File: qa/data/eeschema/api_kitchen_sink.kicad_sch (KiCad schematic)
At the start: 1 part

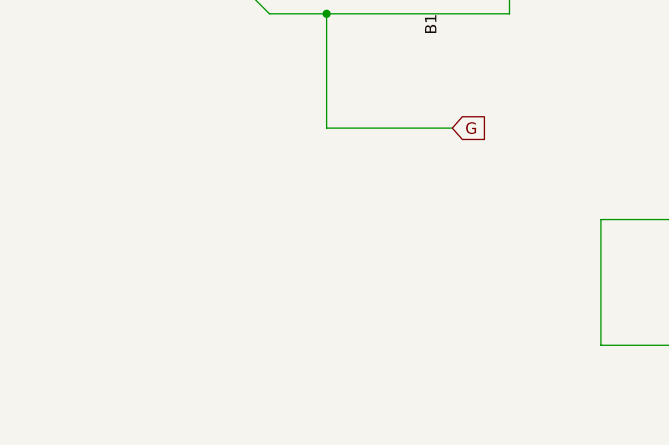
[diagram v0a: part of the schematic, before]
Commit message: API: support symbols and pins
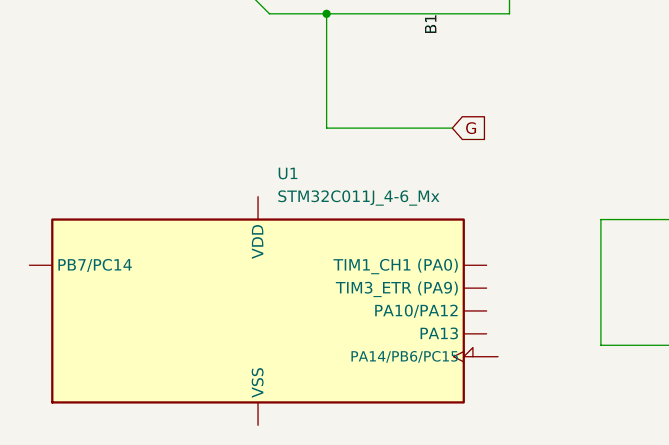
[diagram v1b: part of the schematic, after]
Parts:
- added U1: STM32C011J_4-6_Mx, Package_SO:SOIC-8_3.9x4.9mm_P1.27mm, symbol MCU_ST_STM32C0:STM32C011J_4-6_Mx
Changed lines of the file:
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@@
+	)
+	(symbol
+		(lib_id "MCU_ST_STM32C0:STM32C011J_4-6_Mx")
+		(at 52.07 73.66 0)
+		(unit 1)
+		(body_style 1)
+		(exclude_from_sim no)
+		(in_bom yes)
+		(on_board yes)
+		(in_pos_files no)
+		(dnp no)
+		(fields_autoplaced yes)
+		(property "Reference" "U1"
+			(at 54.2133 58.42 0)
+			(show_name no)
+			(do_not_autoplace no)
+			(effects
+				(font
+					(size 1.27 1.27)
+				)
+				(justify left)
+			)
+		)
+		(property "Value" "STM32C011J_4-6_Mx"
+			(at 54.2133 60.96 0)
+			(show_name no)
+			(do_not_autoplace no)
+			(effects
+				(font
+					(size 1.27 1.27)
+				)
+				(justify left)
+			)
+		)
+		(property "Footprint" "Package_SO:SOIC-8_3.9x4.9mm_P1.27mm"
+			(at 29.21 83.82 0)
+			(hide yes)
+			(show_name no)
+			(do_not_autoplace no)
+			(effects
+				(font
+					(size 1.27 1.27)
+				)
+				(justify right)
+			)
+		)
+		(property "Datasheet" "https://www.st.com/resource/en/datasheet/stm32c011j4.pdf"
+			(at 52.07 73.66 0)
+			(hide yes)
+			(show_name no)
+			(do_not_autoplace no)
+			(effects
+				(font
+					(size 1.27 1.27)
+				)
+			)
+		)
+		(property "Description" "STMicroelectronics Arm Cortex-M0+ MCU, 16-32KB flash, 6KB RAM, 48 MHz, 2.0-3.6V, 6 GPIO, SO8N"
+			(at 52.07 73.66 0)
+			(hide yes)
+			(show_name no)
+			(do_not_autoplace no)
+			(effects
+				(font
+					(size 1.27 1.27)
+				)
+			)
+		)
+		(pin "6"
+		)
+		(pin "7"
+		)
+		(pin "8"
+		)
+		(pin "1"
+		)
+		(pin "2"
+		)
+		(pin "3"
+		)
+		(pin "4"
+			(alternate "TIM1_CH1 (PA0)")
+		)
+		(pin "5"
+			(alternate "TIM3_ETR (PA9)")
+		)
+		(instances
+			(project "api_kitchen_sink"
+				(path "/d6ee7e6a-6570-43fd-93e6-b98f9cea3e37"
+					(reference "U1")
+					(unit 1)
+				)
+			)
+		)
 	)
 	(symbol
